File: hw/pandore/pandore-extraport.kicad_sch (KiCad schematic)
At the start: 0 parts

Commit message: most of board control signals added, routed and defined
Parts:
- added J33: hdr-1x4, footprint, symbol reekilib_con:hdr-1x4

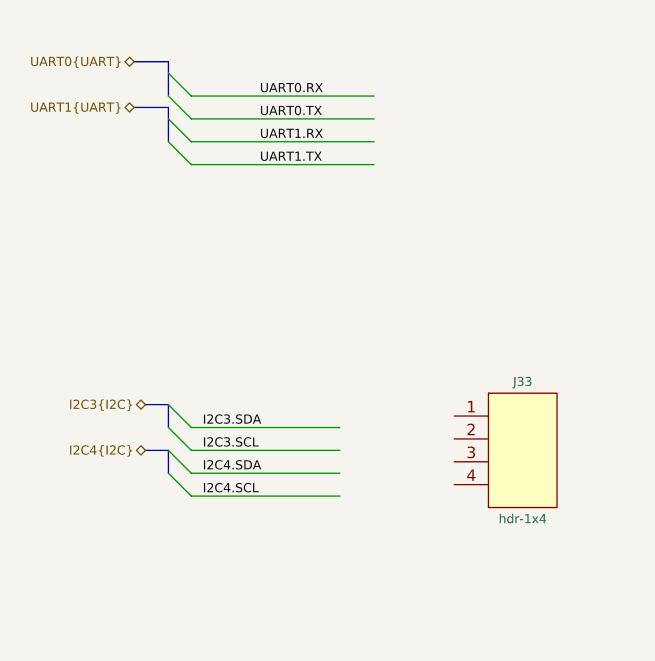
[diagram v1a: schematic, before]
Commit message: more routing/placement done added 5v load switch 1A each added second fan circuit redone all diffpair routing following new stackup calc added all (?) missing connectors to unused pins
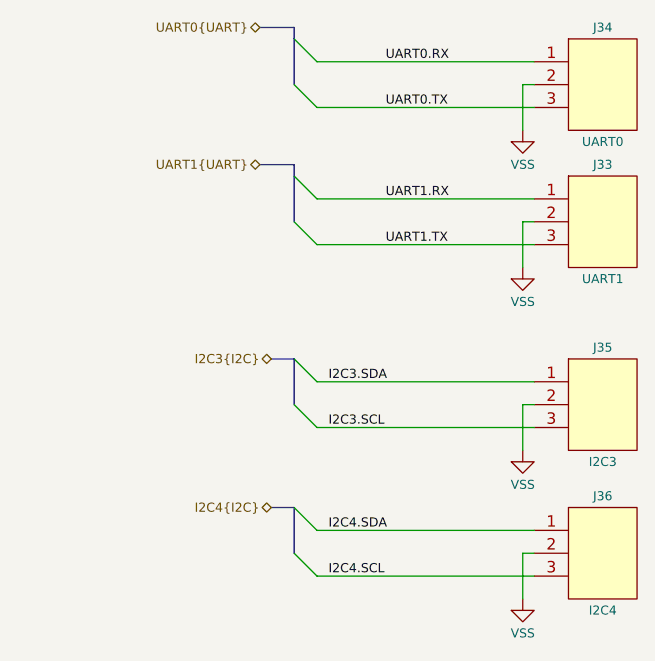
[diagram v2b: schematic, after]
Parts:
- removed J33: hdr-1x4, footprint, symbol reekilib_con:hdr-1x4
- added J33: UART1, reekilib_con:HDR254P1X03-TH, symbol reekilib_con:hdr-1x3
- added J34: UART0, reekilib_con:HDR254P1X03-TH, symbol reekilib_con:hdr-1x3
- added J35: I2C3, reekilib_con:HDR254P1X03-TH, symbol reekilib_con:hdr-1x3
- added J36: I2C4, reekilib_con:HDR254P1X03-TH, symbol reekilib_con:hdr-1x3
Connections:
- net I2C3.SCL: now also J35.3
- net I2C3.SDA: now also J35.1
- net I2C4.SCL: now also J36.3
- net I2C4.SDA: now also J36.1
- net UART0.RX: now also J34.1
- net UART0.TX: now also J34.3
- net UART1.RX: now also J33.1
- net UART1.TX: now also J33.3
- new net VSS: J33.2, J34.2, J35.2, J36.2

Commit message: finished adding mpn,mfg to all parts, finished routing placement
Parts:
- J33, J34, J35, J36: Link url-link -> (none); MFG MFG -> Adam Tech; MPN MPN -> PH1-03-UA
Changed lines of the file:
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@@
 			)
 		)
-		(property "Datasheet" "url-ds"
+		(property "Datasheet" "https://app.adam-tech.com/products/download/data_sheet/201605/ph1-xx-ua-data-sheet.pdf"
 			(at 104.14 110.236 0)
 			(do_not_autoplace yes)
@@
 			)
 		)
-		(property "MPN" "MPN"
+		(property "MPN" "PH1-03-UA"
 			(at 104.14 104.394 0)
 			(do_not_autoplace yes)
@@
 			)
 		)
-		(property "MFG" "MFG"
+		(property "MFG" "Adam Tech"
 			(at 110.744 104.394 0)
 			(do_not_autoplace yes)
@@
 			)
 		)
-		(property "Link" "url-link"
+		(property "Link" ""
 			(at 104.14 108.966 0)
 			(do_not_autoplace yes)
@@
 			)
 		)
-		(property "Datasheet" "url-ds"
+		(property "Datasheet" "https://app.adam-tech.com/products/download/data_sheet/201605/ph1-xx-ua-data-sheet.pdf"
 			(at 104.14 74.676 0)
 			(do_not_autoplace yes)
@@
 			)
 		)
-		(property "MPN" "MPN"
+		(property "MPN" "PH1-03-UA"
 			(at 104.14 68.834 0)
 			(do_not_autoplace yes)
@@
 			)
 		)
-		(property "MFG" "MFG"
+		(property "MFG" "Adam Tech"
 			(at 110.744 68.834 0)
 			(do_not_autoplace yes)
@@
 			)
 		)
-		(property "Link" "url-link"
+		(property "Link" ""
 			(at 104.14 73.406 0)
 			(do_not_autoplace yes)
@@
 			)
 		)
-		(property "Datasheet" "url-ds"
+		(property "Datasheet" "https://app.adam-tech.com/products/download/data_sheet/201605/ph1-xx-ua-data-sheet.pdf"
 			(at 104.14 126.746 0)
 			(do_not_autoplace yes)
@@
 			)
 		)
-		(property "MPN" "MPN"
+		(property "MPN" "PH1-03-UA"
 			(at 104.14 120.904 0)
 			(do_not_autoplace yes)
@@
 			)
 		)
-		(property "MFG" "MFG"
+		(property "MFG" "Adam Tech"
 			(at 110.744 120.904 0)
 			(do_not_autoplace yes)
@@
 			)
 		)
-		(property "Link" "url-link"
+		(property "Link" ""
 			(at 104.14 125.476 0)
 			(do_not_autoplace yes)
@@
 			)
 		)
-		(property "Datasheet" "url-ds"
+		(property "Datasheet" "https://app.adam-tech.com/products/download/data_sheet/201605/ph1-xx-ua-data-sheet.pdf"
 			(at 104.14 89.916 0)
 			(do_not_autoplace yes)
@@
 			)
 		)
-		(property "MPN" "MPN"
+		(property "MPN" "PH1-03-UA"
 			(at 104.14 84.074 0)
 			(do_not_autoplace yes)
@@
 			)
 		)
-		(property "MFG" "MFG"
+		(property "MFG" "Adam Tech"
 			(at 110.744 84.074 0)
 			(do_not_autoplace yes)
@@
 			)
 		)
-		(property "Link" "url-link"
+		(property "Link" ""
 			(at 104.14 88.646 0)
 			(do_not_autoplace yes)
